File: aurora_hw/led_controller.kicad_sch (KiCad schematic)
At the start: 55 parts, among them J1 Screw_Terminal_01x02, J10 Conn_01x03, J2 SJ-3524-SMT, J3 Conn_01x03, J4 Conn_01x03, J5 Conn_01x03, J6 Conn_01x03, J7 Conn_01x03, J8 Conn_01x03, J9 Conn_01x03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

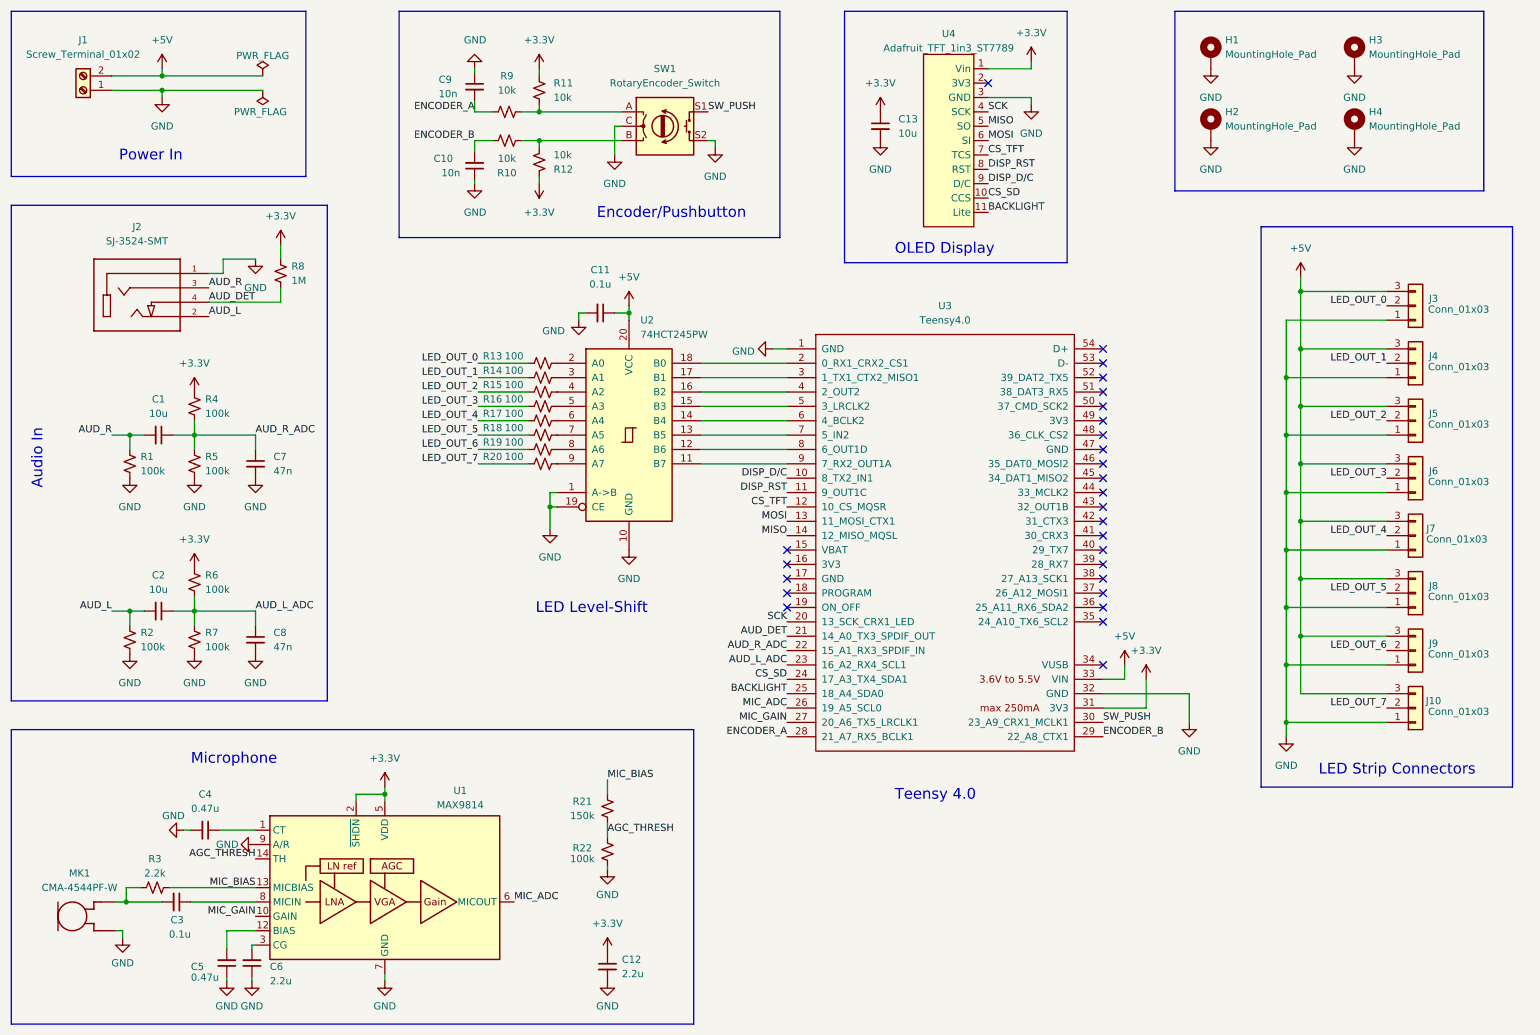
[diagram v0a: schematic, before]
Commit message: Add switch for changing A/R ratio, lengthen DFN pads
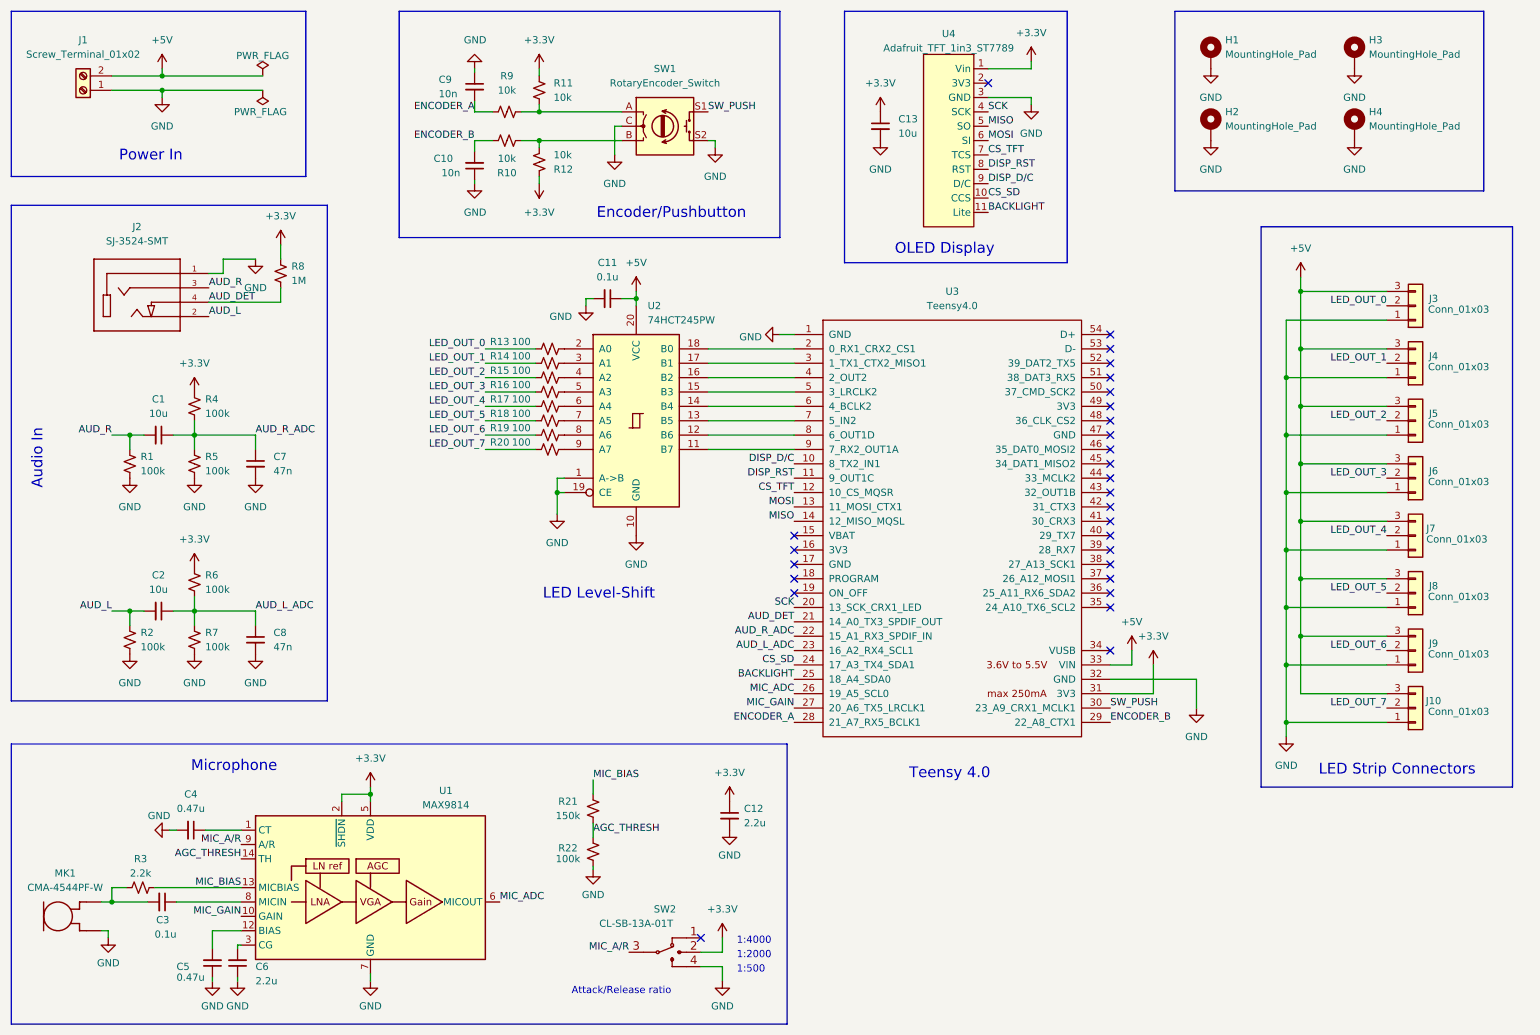
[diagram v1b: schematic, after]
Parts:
- added SW2: CL-SB-13A-01T, SP3T-CL-SB-13A-01T:CL-SB-13A-01T, symbol SP3T-CL-SB-13A-01T:CL-SB-13A-01T
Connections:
- net +3V3: now also SW2.2
- net GND: now also SW2.4; no longer U1.9 (A/R)
- new net MIC_A/R: SW2.3, U1.9 (A/R)
- no-connect marks 27 -> 28
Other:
- note added: "1:2000"
- note added: "1:4000"
- note added: "1:500"
- note added: "Attack/Release ratio"
- moved on the sheet: C11, C12, C3, C4, C5, C6, MK1, R13, R14, R15, R16, R17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

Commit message: Hardware v2
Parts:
- C12: value 2.2u -> 1u
- C3: value 0.1u -> 10u
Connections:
- net +3V3: now also SW2.1; no longer SW2.2
- net GND: now also SW2.2; no longer SW2.4
- net MIC_A/R: now also U3.27 (20_A6_TX5_LRCLK1); no longer SW2.3
- net MIC_GAIN: now also SW2.3; no longer U3.27 (20_A6_TX5_LRCLK1)
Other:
- note added: "40dB"
- note added: "50dB"
- note added: "60dB"
- note added: "Max gain"
- note added: "Tantalum"
- note removed: "1:2000"
- note removed: "1:4000"
- note removed: "1:500"
- note removed: "Attack/Release ratio"
- moved on the sheet: C4
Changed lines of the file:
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@@
   (no_connect (at 210.82 109.22))
   (no_connect (at 154.94 116.84))
-  (no_connect (at 138.43 177.8))
+  (no_connect (at 138.43 182.88))
   (no_connect (at 210.82 73.66))
   (no_connect (at 210.82 91.44))
@@
     (stroke (width 0) (type default) (color 0 0 0 0))
   )
+  (wire (pts (xy 29.21 158.75) (xy 33.02 158.75))
+    (stroke (width 0) (type default) (color 0 0 0 0))
+  )
   (wire (pts (xy 152.4 71.12) (xy 154.94 71.12))
     (stroke (width 0) (type default) (color 0 0 0 0))
@@
     (stroke (width 0) (type default) (color 0 0 0 0))
   )
-  (wire (pts (xy 138.43 180.34) (xy 142.24 180.34))
+  (wire (pts (xy 138.43 177.8) (xy 142.24 177.8))
     (stroke (width 0) (type default) (color 0 0 0 0))
   )
@@
     (stroke (width 0) (type default) (color 0 0 0 0))
   )
-  (wire (pts (xy 142.24 180.34) (xy 142.24 177.8))
+  (wire (pts (xy 142.24 177.8) (xy 142.24 175.26))
     (stroke (width 0) (type default) (color 0 0 0 0))
   )
@@
     (stroke (width 0) (type default) (color 0 0 0 0))
   )
-  (wire (pts (xy 138.43 182.88) (xy 142.24 182.88))
+  (wire (pts (xy 138.43 180.34) (xy 142.24 180.34))
     (stroke (width 0) (type default) (color 0 0 0 0))
   )
@@
     (stroke (width 0) (type default) (color 0 0 0 0))
   )
+  (wire (pts (xy 29.21 158.75) (xy 29.21 160.02))
+    (stroke (width 0) (type default) (color 0 0 0 0))
+  )
   (wire (pts (xy 59.69 120.015) (xy 48.895 120.015))
     (stroke (width 0) (type default) (color 0 0 0 0))
   )
-  (wire (pts (xy 50.8 158.75) (xy 57.15 158.75))
+  (wire (pts (xy 38.1 158.75) (xy 57.15 158.75))
     (stroke (width 0) (type default) (color 0 0 0 0))
   )
@@
     (stroke (width 0) (type default) (color 0 0 0 0))
   )
-  (wire (pts (xy 142.24 182.88) (xy 142.24 185.42))
+  (wire (pts (xy 142.24 180.34) (xy 142.24 182.88))
     (stroke (width 0) (type default) (color 0 0 0 0))
   )
-  (wire (pts (xy 44.45 158.75) (xy 45.72 158.75))
-    (stroke (width 0) (type default) (color 0 0 0 0))
-  )
-  (text "1:2000" (at 144.78 181.61 0)
+  (text "50dB" (at 144.78 181.61 0)
     (effects (font (size 1.27 1.27)) (justify left bottom))
   )
@@
     (effects (font (size 1.905 1.905)) (justify left bottom))
   )
-  (text "Attack/Release ratio" (at 115.57 187.96 0)
+  (text "Max gain" (at 123.19 187.96 0)
+    (effects (font (size 1.27 1.27)) (justify left bottom))
+  )
+  (text "Tantalum" (at 39.37 180.34 0)
     (effects (font (size 1.27 1.27)) (justify left bottom))
   )
-  (text "1:500" (at 144.78 184.15 0)
+  (text "60dB" (at 144.78 184.15 0)
     (effects (font (size 1.27 1.27)) (justify left bottom))
   )
@@
     (effects (font (size 1.905 1.905)) (justify left bottom))
   )
-  (text "1:4000" (at 144.78 179.07 0)
+  (text "40dB" (at 144.78 179.07 0)
     (effects (font (size 1.27 1.27)) (justify left bottom))
   )
@@
     (effects (font (size 1.27 1.27)) (justify right bottom))
   )
-  (label "MIC_GAIN" (at 154.94 137.16 180)
+  (label "MIC_GAIN" (at 125.73 180.34 180)
     (effects (font (size 1.27 1.27)) (justify right bottom))
   )
@@
     (effects (font (size 1.27 1.27)) (justify left bottom))
   )
-  (label "MIC_A{slash}R" (at 125.73 180.34 180)
+  (label "MIC_A{slash}R" (at 154.94 137.16 180)
     (effects (font (size 1.27 1.27)) (justify right bottom))
   )
@@
       (effects (font (size 1.27 1.27)) (justify right))
     )
-    (property "Value" "0.1u" (id 1) (at 45.72 177.165 90)
+    (property "Value" "10u" (id 1) (at 45.72 177.165 90)
       (effects (font (size 1.27 1.27)) (justify right))
     )
@@
     (pin "1")
   )
-  (symbol (lib_id "power:GND") (at 44.45 158.75 270) (unit 1)
+  (symbol (lib_id "power:GND") (at 29.21 160.02 0) (unit 1)
     (in_bom yes) (on_board yes)
-    (property "Reference" "#PWR06" (id 0) (at 38.1 158.75 0)
+    (property "Reference" "#PWR06" (id 0) (at 29.21 166.37 0)
       (effects (font (size 1.27 1.27)) hide)
     )
-    (property "Value" "GND" (id 1) (at 40.64 156.21 90)
+    (property "Value" "GND" (id 1) (at 22.86 161.29 0)
       (effects (font (size 1.27 1.27)) (justify left))
     )
-    (property "Footprint" "" (id 2) (at 44.45 158.75 0)
+    (property "Footprint" "" (id 2) (at 29.21 160.02 0)
       (effects (font (size 1.27 1.27)) hide)
     )
-    (property "Datasheet" "" (id 3) (at 44.45 158.75 0)
+    (property "Datasheet" "" (id 3) (at 29.21 160.02 0)
       (effects (font (size 1.27 1.27)) hide)
     )
@@
     (pin "3")
   )
-  (symbol (lib_id "Device:C_Small") (at 48.26 158.75 270) (unit 1)
+  (symbol (lib_id "Device:C_Small") (at 35.56 158.75 270) (unit 1)
     (in_bom yes) (on_board yes) (fields_autoplaced)
-    (property "Reference" "C4" (id 0) (at 48.2536 152.4 90))
-    (property "Value" "0.47u" (id 1) (at 48.2536 154.94 90))
-    (property "Footprint" "Capacitor_SMD:C_0805_2012Metric_Pad1.18x1.45mm_HandSolder" (id 2) (at 48.26 158.75 0)
+    (property "Reference" "C4" (id 0) (at 35.5536 152.4 90))
+    (property "Value" "0.47u" (id 1) (at 35.5536 154.94 90))
+    (property "Footprint" "Capacitor_SMD:C_0805_2012Metric_Pad1.18x1.45mm_HandSolder" (id 2) (at 35.56 158.75 0)
       (effects (font (size 1.27 1.27)) hide)
     )
-    (property "Datasheet" "~" (id 3) (at 48.26 158.75 0)
+    (property "Datasheet" "~" (id 3) (at 35.56 158.75 0)
       (effects (font (size 1.27 1.27)) hide)
     )
-    (property "Package" "0805" (id 4) (at 48.26 158.75 0)
+    (property "Package" "0805" (id 4) (at 35.56 158.75 0)
       (effects (font (size 1.27 1.27)) hide)
     )
-    (property "Layer" "B" (id 5) (at 48.26 158.75 0)
+    (property "Layer" "B" (id 5) (at 35.56 158.75 0)
       (effects (font (size 1.27 1.27)) hide)
     )
-    (property "LCSC Part Number" "C13967" (id 6) (at 48.26 158.75 0)
+    (property "LCSC Part Number" "C13967" (id 6) (at 35.56 158.75 0)
       (effects (font (size 1.27 1.27)) hide)
     )
@@
     (pin "2")
   )
-  (symbol (lib_id "power:GND") (at 142.24 185.42 0) (unit 1)
+  (symbol (lib_id "power:GND") (at 142.24 182.88 0) (unit 1)
     (in_bom yes) (on_board yes) (fields_autoplaced)
-    (property "Reference" "#PWR0102" (id 0) (at 142.24 191.77 0)
+    (property "Reference" "#PWR0102" (id 0) (at 142.24 189.23 0)
       (effects (font (size 1.27 1.27)) hide)
     )
-    (property "Value" "GND" (id 1) (at 142.24 189.865 0))
-    (property "Footprint" "" (id 2) (at 142.24 185.42 0)
+    (property "Value" "GND" (id 1) (at 142.24 187.325 0))
+    (property "Footprint" "" (id 2) (at 142.24 182.88 0)
       (effects (font (size 1.27 1.27)) hide)
     )
-    (property "Datasheet" "" (id 3) (at 142.24 185.42 0)
+    (property "Datasheet" "" (id 3) (at 142.24 182.88 0)
       (effects (font (size 1.27 1.27)) hide)
     )
@@
     (pin "2")
   )
-  (symbol (lib_id "power:+3.3V") (at 142.24 177.8 0) (unit 1)
+  (symbol (lib_id "power:+3.3V") (at 142.24 175.26 0) (unit 1)
     (in_bom yes) (on_board yes) (fields_autoplaced)
-    (property "Reference" "#PWR0101" (id 0) (at 142.24 181.61 0)
+    (property "Reference" "#PWR0101" (id 0) (at 142.24 179.07 0)
       (effects (font (size 1.27 1.27)) hide)
     )
-    (property "Value" "+3.3V" (id 1) (at 142.24 172.72 0))
-    (property "Footprint" "" (id 2) (at 142.24 177.8 0)
+    (property "Value" "+3.3V" (id 1) (at 142.24 170.18 0))
+    (property "Footprint" "" (id 2) (at 142.24 175.26 0)
       (effects (font (size 1.27 1.27)) hide)
     )
-    (property "Datasheet" "" (id 3) (at 142.24 177.8 0)
+    (property "Datasheet" "" (id 3) (at 142.24 175.26 0)
       (effects (font (size 1.27 1.27)) hide)
     )
@@
   )
   (symbol (lib_id "CMA-4544PF-W:CMA-4544PF-W") (at 24.765 173.99 0) (unit 1)
-    (in_bom yes) (on_board yes) (fields_autoplaced)
+    (in_bom yes) (on_board yes)
     (property "Reference" "MK1" (id 0) (at 26.035 166.37 0))
     (property "Value" "CMA-4544PF-W" (id 1) (at 26.035 168.91 0))
@@
       (effects (font (size 1.27 1.27)) (justify left))
     )
-    (property "Value" "2.2u" (id 1) (at 146.05 157.4862 0)
+    (property "Value" "1u" (id 1) (at 146.05 157.4862 0)
       (effects (font (size 1.27 1.27)) (justify left))
     )
@@
     )
     (path "/1bc1c98b-0492-434e-a083-3385b8b5dfb7"
-      (reference "C3") (unit 1) (value "0.1u") (footprint "Capacitor_SMD:C_0805_2012Metric_Pad1.18x1.45mm_HandSolder")
+      (reference "C3") (unit 1) (value "10u") (footprint "Capacitor_SMD:C_0805_2012Metric_Pad1.18x1.45mm_HandSolder")
     )
     (path "/5a9cf46d-6415-426d-ad2b-321300b09d80"
@@
     )
     (path "/c60d9e0d-f785-47a3-ba4d-3be6083682de"
-      (reference "C12") (unit 1) (value "2.2u") (footprint "Capacitor_SMD:C_0805_2012Metric_Pad1.18x1.45mm_HandSolder")
+      (reference "C12") (unit 1) (value "1u") (footprint "Capacitor_SMD:C_0805_2012Metric_Pad1.18x1.45mm_HandSolder")
     )
     (path "/236630a8-25c7-46f9-b759-013868a485a5"
